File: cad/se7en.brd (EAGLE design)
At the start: 64 x 34 mm, 67 parts, among them CN1 MICROSD-EJECT, CN3 DO NOT PLACE, CN4 DO NOT PLACE, CN5 DO NOT PLACE, CN6 DO NOT PLACE, CN7 DO NOT PLACE, Q1 FDC6329S, SW1 SWITCHKMR211, SW2 SWITCHKMR211, U1 ATSAME70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

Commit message: tweak
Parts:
- U1: value ATSAME70 -> ATSAMS70
- renumbered LOGO1 to LOGO$1
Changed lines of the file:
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@@
 <grid distance="0.1" unitdist="mm" unit="mm" style="lines" multiple="5" display="yes" altdistance="0.025" altunitdist="inch" altunit="inch"/>
 <layers>
-<layer number="1" name="Top" color="4" fill="1" visible="yes" active="yes"/>
+<layer number="1" name="Top" color="4" fill="1" visible="no" active="yes"/>
 <layer number="2" name="Route2" color="6" fill="1" visible="no" active="yes"/>
 <layer number="3" name="Route3" color="4" fill="3" visible="no" active="no"/>
 <layer number="14" name="Route14" color="1" fill="6" visible="no" active="no"/>
 <layer number="15" name="Route15" color="13" fill="1" visible="no" active="yes"/>
-<layer number="16" name="Bottom" color="1" fill="1" visible="yes" active="yes"/>
+<layer number="16" name="Bottom" color="1" fill="1" visible="no" active="yes"/>
 <layer number="17" name="Pads" color="2" fill="1" visible="yes" active="yes"/>
 <layer number="18" name="Vias" color="2" fill="1" visible="yes" active="yes"/>
@@
 <layer number="23" name="tOrigins" color="15" fill="1" visible="yes" active="yes"/>
 <layer number="24" name="bOrigins" color="15" fill="1" visible="yes" active="yes"/>
-<layer number="25" name="tNames" color="7" fill="1" visible="no" active="yes"/>
+<layer number="25" name="tNames" color="7" fill="1" visible="yes" active="yes"/>
 <layer number="26" name="bNames" color="7" fill="1" visible="yes" active="yes"/>
 <layer number="27" name="tValues" color="7" fill="1" visible="no" active="yes"/>
@@
 </autorouter>
 <elements>
-<element name="U1" library="jaw" package="TQFP-100-14X14MM" value="ATSAME70" x="89" y="53" smashed="yes">
+<element name="U1" library="jaw" package="TQFP-100-14X14MM" value="ATSAMS70" x="89" y="53" smashed="yes">
 <attribute name="NAME" x="79.5" y="60" size="1" layer="25" ratio="10"/>
 <attribute name="VALUE" x="85" y="49" size="1" layer="27" ratio="10"/>
@@
 <element name="U$1" library="jaw" package="ROBOTMAN-LOGO2" value="ROBOTMAN-LOGO2" x="91.2" y="58.4" rot="MR0"/>
 <element name="U$3" library="jaw" package="ROBOTMAN-LOGO2" value="ROBOTMAN-LOGO2" x="70.1" y="48"/>
-<element name="LOGO1" library="SparkFun-Aesthetics" package="OSHW-LOGO-M" value="OSHW-LOGOM" x="97.9" y="55.7" rot="MR0"/>
+<element name="LOGO$1" library="SparkFun-Aesthetics" package="OSHW-LOGO-M" value="OSHW-LOGOM" x="97.9" y="55.7" rot="MR0"/>
 <element name="U2" library="jaw" package="SOT-23-5" value="MCP73831" x="59.5" y="60" smashed="yes" rot="R90">
 <attribute name="NAME" x="58.305" y="60.395" size="0.75" layer="25" ratio="10" rot="R180"/>

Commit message: fix typo
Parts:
- Q1: value FDC6329S -> FDC6392S
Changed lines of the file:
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@@
 <layer number="23" name="tOrigins" color="15" fill="1" visible="yes" active="yes"/>
 <layer number="24" name="bOrigins" color="15" fill="1" visible="yes" active="yes"/>
-<layer number="25" name="tNames" color="7" fill="1" visible="yes" active="yes"/>
+<layer number="25" name="tNames" color="7" fill="1" visible="no" active="yes"/>
 <layer number="26" name="bNames" color="7" fill="1" visible="yes" active="yes"/>
-<layer number="27" name="tValues" color="7" fill="1" visible="no" active="yes"/>
+<layer number="27" name="tValues" color="7" fill="1" visible="yes" active="yes"/>
 <layer number="28" name="bValues" color="7" fill="1" visible="yes" active="yes"/>
 <layer number="29" name="tStop" color="7" fill="3" visible="no" active="yes"/>
@@
 <attribute name="VALUE" x="100.122" y="33.714" size="1" layer="27" font="vector" ratio="10"/>
 </element>
-<element name="Q1" library="jaw" package="SOT-23-6" value="FDC6329S" x="63" y="60" smashed="yes" rot="R270">
+<element name="Q1" library="jaw" package="SOT-23-6" value="FDC6392S" x="63" y="60" smashed="yes" rot="R270">
 <attribute name="NAME" x="64.7" y="60.5" size="0.75" layer="25" ratio="10" rot="R270"/>
 <attribute name="VALUE" x="61.6" y="59.7" size="0.5" layer="27"/>

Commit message: tweak orientation
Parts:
- moved CN1 0.50 mm to (110.0, 50.5), turned to 270 degrees
- turned LED2 to 90 degrees
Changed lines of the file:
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@@
 <grid distance="0.1" unitdist="mm" unit="mm" style="lines" multiple="5" display="yes" altdistance="0.025" altunitdist="inch" altunit="inch"/>
 <layers>
-<layer number="1" name="Top" color="4" fill="1" visible="no" active="yes"/>
+<layer number="1" name="Top" color="4" fill="1" visible="yes" active="yes"/>
 <layer number="2" name="Route2" color="6" fill="1" visible="no" active="yes"/>
 <layer number="3" name="Route3" color="4" fill="3" visible="no" active="no"/>
 <layer number="14" name="Route14" color="1" fill="6" visible="no" active="no"/>
 <layer number="15" name="Route15" color="13" fill="1" visible="no" active="yes"/>
-<layer number="16" name="Bottom" color="1" fill="1" visible="no" active="yes"/>
+<layer number="16" name="Bottom" color="1" fill="1" visible="yes" active="yes"/>
 <layer number="17" name="Pads" color="2" fill="1" visible="yes" active="yes"/>
 <layer number="18" name="Vias" color="2" fill="1" visible="yes" active="yes"/>
@@
 <layer number="23" name="tOrigins" color="15" fill="1" visible="yes" active="yes"/>
 <layer number="24" name="bOrigins" color="15" fill="1" visible="yes" active="yes"/>
-<layer number="25" name="tNames" color="7" fill="1" visible="no" active="yes"/>
+<layer number="25" name="tNames" color="7" fill="1" visible="yes" active="yes"/>
 <layer number="26" name="bNames" color="7" fill="1" visible="yes" active="yes"/>
-<layer number="27" name="tValues" color="7" fill="1" visible="yes" active="yes"/>
+<layer number="27" name="tValues" color="7" fill="1" visible="no" active="yes"/>
 <layer number="28" name="bValues" color="7" fill="1" visible="yes" active="yes"/>
 <layer number="29" name="tStop" color="7" fill="3" visible="no" active="yes"/>
@@
 <layer number="49" name="Reference" color="7" fill="1" visible="yes" active="yes"/>
 <layer number="50" name="dxf" color="7" fill="1" visible="no" active="no"/>
-<layer number="51" name="tDocu" color="7" fill="1" visible="no" active="yes"/>
+<layer number="51" name="tDocu" color="7" fill="1" visible="yes" active="yes"/>
 <layer number="52" name="bDocu" color="7" fill="1" visible="yes" active="yes"/>
 <layer number="53" name="tGND_GNDA" color="7" fill="1" visible="no" active="no"/>
@@
 <attribute name="VALUE" x="74" y="71" size="1.778" layer="27" rot="R180" display="off"/>
 </element>
-<element name="CN1" library="jaw" package="MICROSD/EJECTOR" value="MICROSD-EJECT" x="110.5" y="50.5" smashed="yes" rot="R90">
-<attribute name="NAME" x="107.1" y="47.2" size="1.27" layer="25" rot="R90" display="off"/>
+<element name="CN1" library="jaw" package="MICROSD/EJECTOR" value="MICROSD-EJECT" x="110" y="50.5" smashed="yes" rot="R270">
+<attribute name="NAME" x="113.4" y="53.8" size="1.27" layer="25" rot="R270" display="off"/>
 </element>
 <element name="C19" library="jaw" package="SMD0402" value=".1u" x="78" y="55.5" smashed="yes">
@@
 <attribute name="VALUE" x="110.4" y="41.9" size="1" layer="27" font="vector" ratio="10" rot="R90"/>
 </element>
-<element name="LED2" library="jaw" package="SMD0805-DUAL" value="LED-DUAL0805" x="110.5" y="37.5" smashed="yes" rot="R270">
-<attribute name="NAME" x="109.722" y="35.116" size="0.5" layer="25" font="vector" ratio="10"/>
-<attribute name="VALUE" x="100.122" y="33.714" size="1" layer="27" font="vector" ratio="10"/>
+<element name="LED2" library="jaw" package="SMD0805-DUAL" value="LED-DUAL0805" x="110.5" y="37.5" smashed="yes" rot="R90">
+<attribute name="NAME" x="111.378" y="35.584" size="0.5" layer="25" font="vector" ratio="10" rot="R180"/>
+<attribute name="VALUE" x="120.878" y="41.286" size="1" layer="27" font="vector" ratio="10" rot="R270" display="off"/>
 </element>
 <element name="Q1" library="jaw" package="SOT-23-6" value="FDC6392S" x="63" y="60" smashed="yes" rot="R270">
@@
 <contactref element="C24" pad="1"/>
 <via x="102" y="51.5" extent="1-16" drill="0.35"/>
-<wire x1="103.4" y1="51.46" x2="102.04" y2="51.46" width="0.25" layer="1"/>
+<wire x1="103.6" y1="51.46" x2="102.04" y2="51.46" width="0.25" layer="1"/>
 <wire x1="102.04" y1="51.46" x2="102" y2="51.5" width="0.25" layer="1"/>
 <via x="112.5" y="47" extent="1-16" drill="0.35"/>
-<wire x1="114" y1="47" x2="113.9" y2="47" width="0.25" layer="1"/>
+<wire x1="114.2" y1="47" x2="113.9" y2="47" width="0.25" layer="1"/>
 <wire x1="113.9" y1="47" x2="112.5" y2="47" width="0.25" layer="1"/>
 <contactref element="CN4" pad="3"/>
@@
 <via x="70" y="55" extent="1-16" drill="0.5"/>
 <via x="69.9" y="56.5" extent="1-16" drill="0.5"/>
-<wire x1="114" y1="49.2" x2="117.4" y2="49.2" width="0.35" layer="1"/>
+<wire x1="114.2" y1="49.2" x2="117.4" y2="49.2" width="0.35" layer="1"/>
 <wire x1="117.4" y1="49.2" x2="117.8" y2="49.6" width="0.35" layer="1"/>
 <wire x1="117.8" y1="49.6" x2="117.8" y2="50.8" width="0.35" layer="1"/>
@@
 <wire x1="110.3" y1="46.9" x2="111.2" y2="46" width="0.25" layer="1"/>
 <wire x1="111.2" y1="46" x2="113.5" y2="46" width="0.25" layer="1"/>
-<wire x1="113.5" y1="46" x2="113.6" y2="45.9" width="0.25" layer="1"/>
+<wire x1="113.5" y1="46" x2="113.8" y2="45.9" width="0.25" layer="1"/>
 <wire x1="111.8" y1="58.8" x2="111.8" y2="54.5" width="0.25" layer="1"/>
 <via x="111.8" y="54.5" extent="1-16" drill="0.35"/>
@@
 <wire x1="109.6" y1="53.7" x2="109.6" y2="46.2" width="0.25" layer="1"/>
 <wire x1="109.6" y1="46.2" x2="111" y2="44.8" width="0.25" layer="1"/>
-<wire x1="111" y1="44.8" x2="113.6" y2="44.8" width="0.25" layer="1"/>
+<wire x1="111" y1="44.8" x2="113.8" y2="44.8" width="0.25" layer="1"/>
 <wire x1="112.6" y1="58.8" x2="112.6" y2="54" width="0.25" layer="1"/>
 <wire x1="112.6" y1="54" x2="112.3" y2="53.7" width="0.25" layer="1"/>
@@
 <via x="112.2" y="52.5" extent="1-16" drill="0.35"/>
 <wire x1="112.2" y1="52.5" x2="113.56" y2="52.5" width="0.25" layer="1"/>
-<wire x1="113.56" y1="52.5" x2="113.6" y2="52.46" width="0.25" layer="1"/>
+<wire x1="113.56" y1="52.5" x2="113.8" y2="52.46" width="0.25" layer="1"/>
 <wire x1="91.5" y1="52.5" x2="92" y2="53" width="0.25" layer="16"/>
 <wire x1="92" y1="53" x2="111.7" y2="53" width="0.25" layer="16"/>
 <wire x1="111.7" y1="53" x2="112.2" y2="52.5" width="0.25" layer="16"/>
-<wire x1="113.4" y1="52.66" x2="113.6" y2="52.46" width="0.35" layer="1"/>
+<wire x1="113.4" y1="52.66" x2="113.8" y2="52.46" width="0.35" layer="1"/>
 <wire x1="113.4" y1="52.66" x2="113.4" y2="58.8" width="0.25" layer="1"/>
 </signal>
@@
 <via x="111.7" y="51.4" extent="1-16" drill="0.35"/>
 <wire x1="111.7" y1="51.4" x2="111.74" y2="51.36" width="0.25" layer="1"/>
-<wire x1="111.74" y1="51.36" x2="113.2" y2="51.36" width="0.25" layer="1"/>
-<wire x1="113.2" y1="51.36" x2="114.46" y2="51.36" width="0.25" layer="1"/>
+<wire x1="111.74" y1="51.36" x2="113.4" y2="51.36" width="0.25" layer="1"/>
+<wire x1="113.4" y1="51.36" x2="114.46" y2="51.36" width="0.25" layer="1"/>
 <wire x1="114.46" y1="51.36" x2="115" y2="51.9" width="0.25" layer="1"/>
 <wire x1="95" y1="45" x2="95" y2="46.5" width="0.25" layer="1"/>
@@
 <wire x1="111.9" y1="48" x2="112" y2="48.1" width="0.25" layer="16"/>
 <via x="112" y="48.1" extent="1-16" drill="0.35"/>
-<wire x1="112" y1="48.1" x2="113.6" y2="48.1" width="0.25" layer="1"/>
+<wire x1="112" y1="48.1" x2="113.8" y2="48.1" width="0.25" layer="1"/>
 <wire x1="90" y1="48" x2="91.3" y2="49.3" width="0.25" layer="16"/>
 <wire x1="91.3" y1="49.3" x2="110" y2="49.3" width="0.25" layer="16"/>
@@
 <wire x1="111" y1="56" x2="111" y2="50.7" width="0.25" layer="1"/>
 <wire x1="111" y1="50.7" x2="111.4" y2="50.3" width="0.25" layer="1"/>
-<wire x1="111.4" y1="50.3" x2="113.6" y2="50.3" width="0.25" layer="1"/>
+<wire x1="111.4" y1="50.3" x2="113.8" y2="50.3" width="0.25" layer="1"/>
 <contactref element="R6" pad="8"/>
 <wire x1="111" y1="56" x2="111" y2="57.7" width="0.25" layer="1"/>
@@
 <signal name="CARDIO">
 <contactref element="CN1" pad="CD1"/>
-<wire x1="108" y1="45.5" x2="103.4" y2="45.5" width="0.25" layer="1"/>
+<wire x1="108" y1="45.5" x2="103.6" y2="45.5" width="0.25" layer="1"/>
 <contactref element="R6" pad="7"/>
 <wire x1="109.9" y1="58.8" x2="109.9" y2="55.8" width="0.25" layer="1"/>

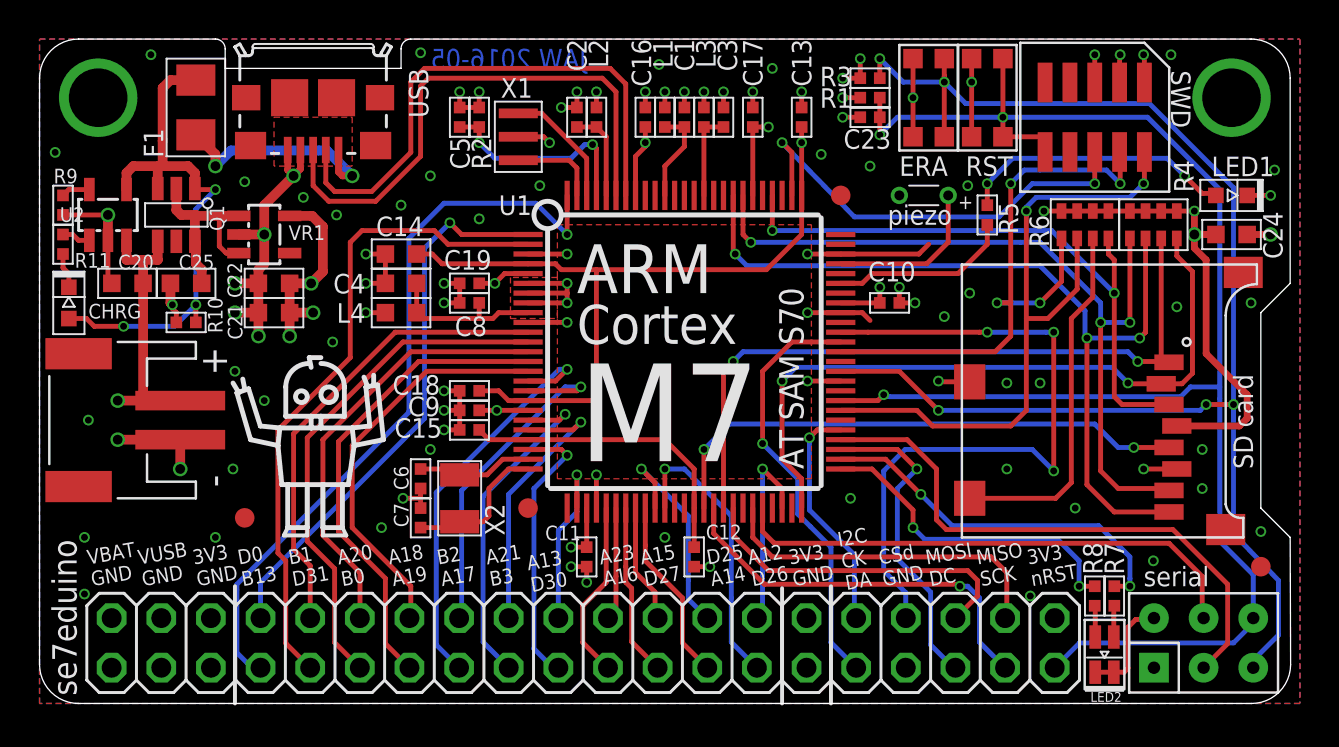
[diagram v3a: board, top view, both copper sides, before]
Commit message: scootch back from edge, tweak silk
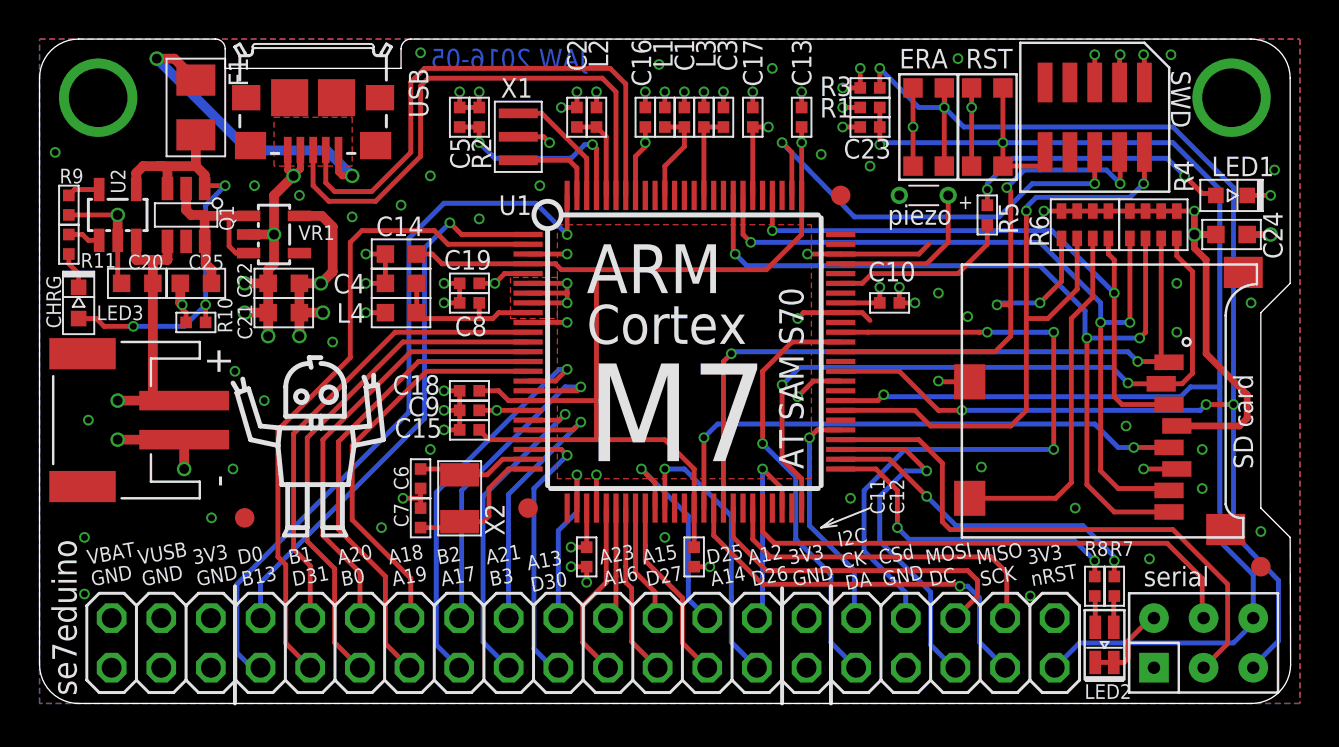
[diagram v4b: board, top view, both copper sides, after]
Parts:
- moved SW1 1.50 mm to (104.5, 64.5)
- moved SW2 1.50 mm to (101.5, 64.5)
- moved LOGO$1 0.82 mm to (97.1, 55.5)
- moved C20 0.50 mm to (61.0, 56.5)
- moved C21 0.50 mm to (68.5, 55.0)
- moved C22 0.50 mm to (68.5, 56.5)
- moved C23 0.50 mm to (98.5, 64.5)
- moved C25 0.50 mm to (64.0, 56.5)
- moved LED2 0.50 mm to (110.5, 38.0)
- moved LED3 0.50 mm to (58.0, 55.5)
- moved Q1 0.50 mm to (63.5, 60.0)
- moved R1 0.50 mm to (98.5, 65.5)
- moved R10 0.50 mm to (64.0, 54.5)
- moved R3 0.50 mm to (98.5, 66.5)
- moved R7 0.50 mm to (111.0, 41.0)
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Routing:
- net VUSB: track 101.5 -> 108.2 mm
- net VIN: track 27.9 -> 24.2 mm
- net IOLED3: track 19.2 -> 17.1 mm
- net CSDC: track 16.2 -> 18.2 mm
- net NRST: track 82.0 -> 81.1 mm
- net GND: track 99.6 -> 100.4 mm, vias 92 -> 91
- net CSDPY: track 35.6 -> 34.9 mm
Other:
- board text added: "Designed in Philly Built by robots"
- board text added: "www.AMIKETO.com"
- board text removed: "www.amiketo.com"

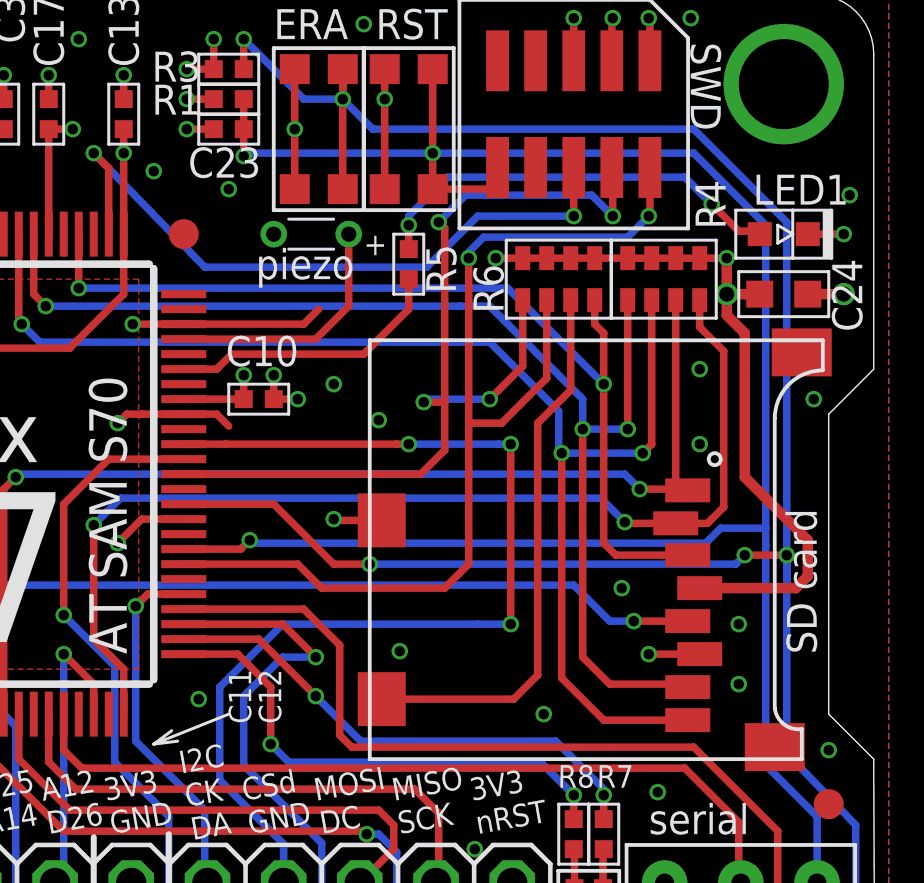
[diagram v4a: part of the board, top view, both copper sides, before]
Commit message: remove pullups (use pio pullups)
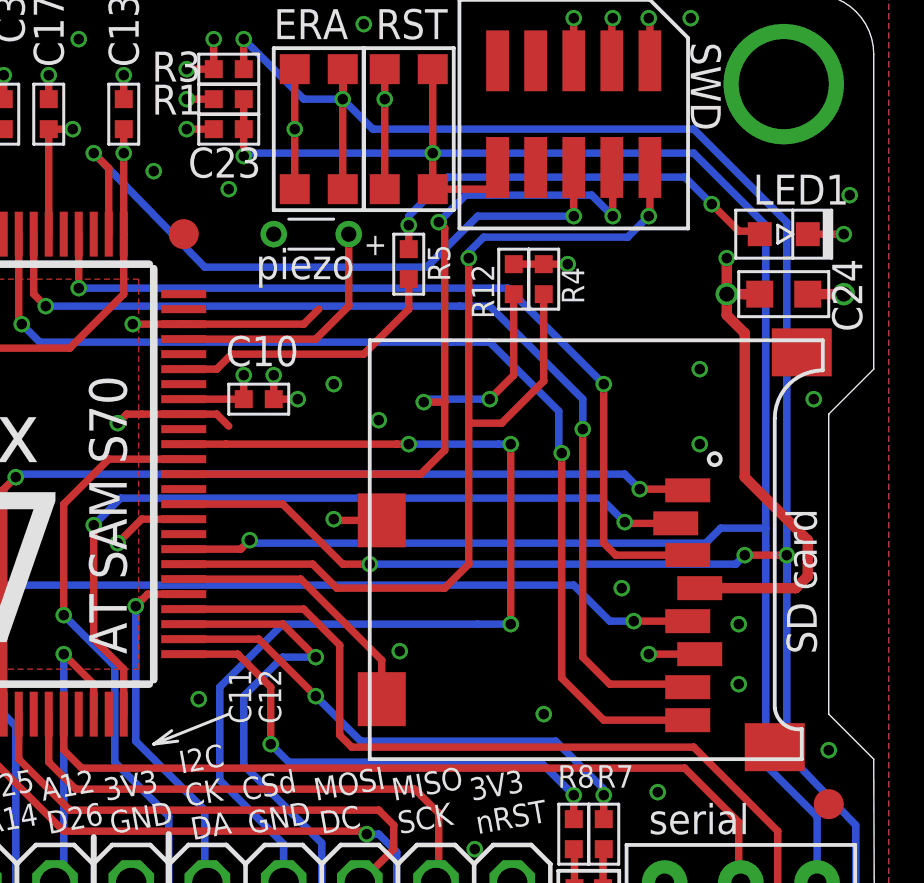
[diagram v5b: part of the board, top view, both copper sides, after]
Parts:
- removed R6: 100k, jaw:SMD-0603-ARV
- added R12: 100k, jaw:SMD0402
- C25: value 10u -> 10u 10V
- L4: value 10u -> 10uH
- R4: device jaw:SMD-0603-ARV -> jaw:SMD0402
- moved R4 4.00 mm to (109.0, 59.5), turned to 90 degrees
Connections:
- net CARDIO: now also U1.56; no longer R6.7
- net SDIOCM: no longer R6.8
- net SDIOD0: no longer R4.5
- net SDIOD1: no longer R4.6
- net SDIOD2: no longer R4.7
- net SDIOD3: no longer R4.8
- net SWCLK: now also R12.1; no longer R6.5
- net SWDIO: now also R4.1; no longer R6.6
- net VCC: now also R12.2; no longer R4.1, R4.3, R4.4, R6.1, R6.2, R6.3, R6.4
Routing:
- net CARDIO: track 18.5 -> 9.02 mm
- net SDIOD3: track 35.9 -> 26.8 mm
- net SDIOD1: track 43.8 -> 35.9 mm, vias 3 -> 2
- net SDIOD2: track 37.3 -> 31.2 mm
- net VCC: track 61.3 -> 55.4 mm
- net SDIOD0: track 40.0 -> 34.2 mm, vias 3 -> 2
- net SDIOCM: track 31.8 -> 28.9 mm

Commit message: tweak
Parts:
- C20, C21, C4: value 10u -> 4u7
- moved R12 0.50 mm to (107.5, 59.5)
- moved R4 0.50 mm to (108.5, 59.5)
- moved R5 0.50 mm to (104.5, 59.5)
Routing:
- net VCC: track 55.4 -> 54.3 mm, vias 17 -> 16
- net N$16: track 14.1 -> 14.6 mm
- net GND: vias 91 -> 92
